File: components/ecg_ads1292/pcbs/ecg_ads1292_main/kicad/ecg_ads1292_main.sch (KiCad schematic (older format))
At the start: 13 parts, among them J1 Conn_02x04_Odd_Even, P1 Conn_02x20_Odd_Even

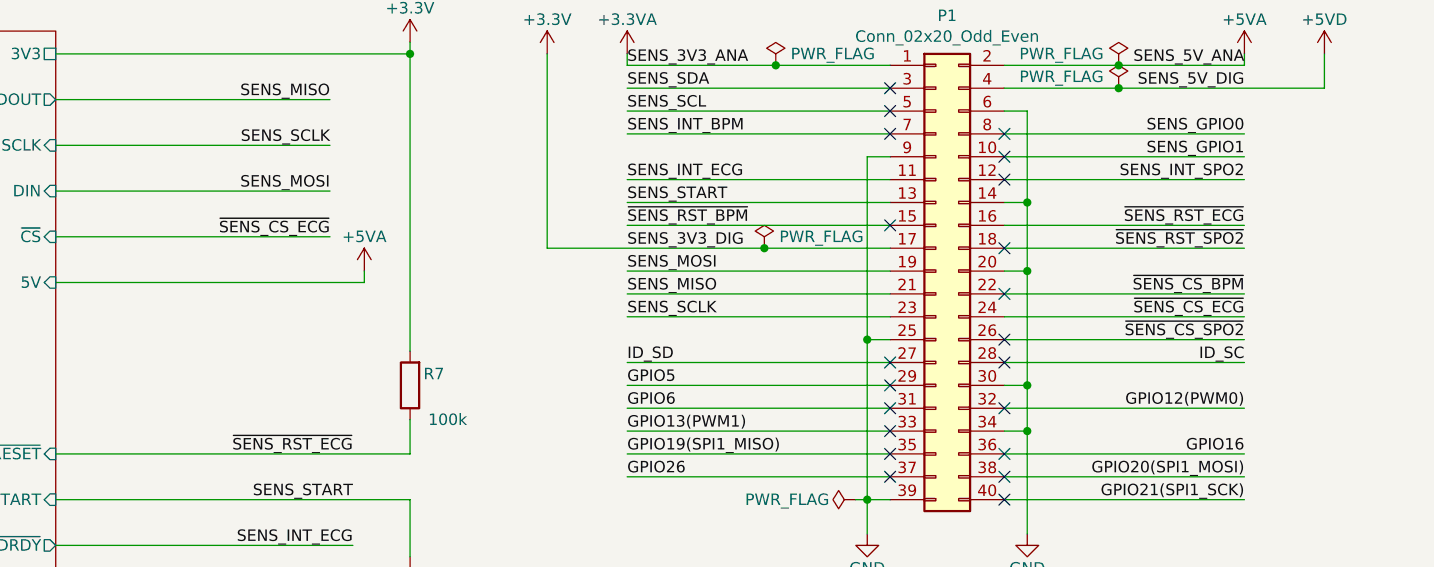
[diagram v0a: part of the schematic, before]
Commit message: add chip select mux in ads1292_main schematics
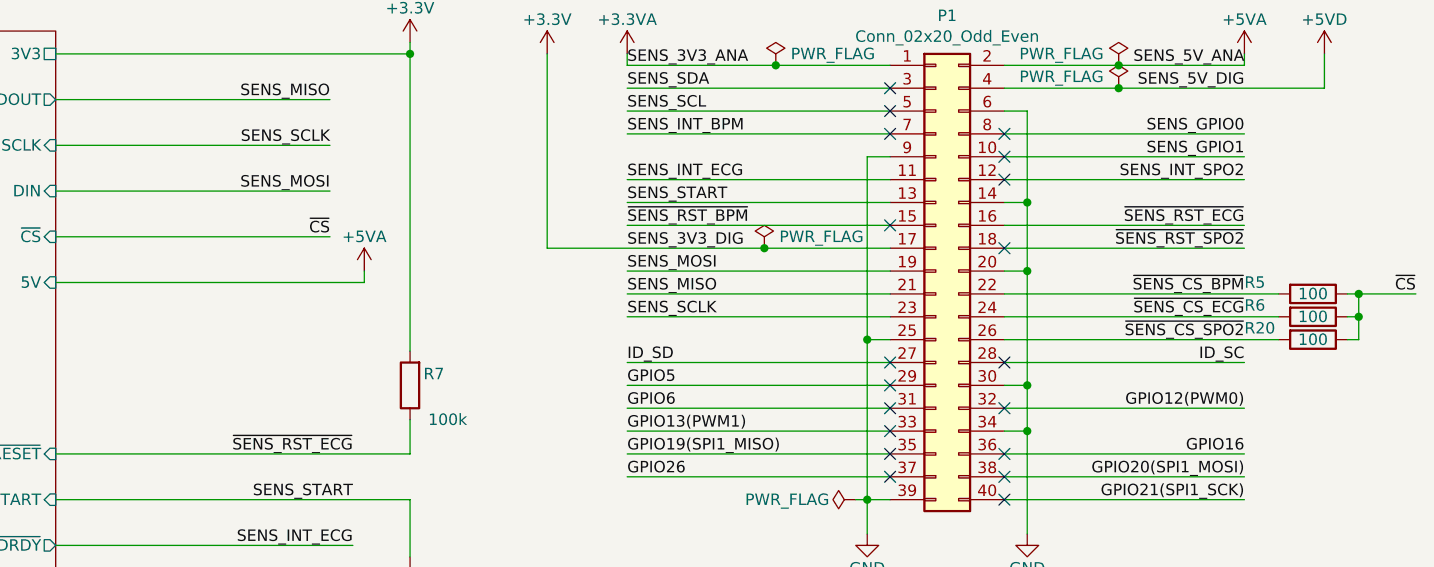
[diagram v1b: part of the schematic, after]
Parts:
- added R20, R5, R6: 100, Resistor_SMD:R_0603_1608Metric_Pad1.05x0.95mm_HandSolder, symbol component:R
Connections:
- net ~SENS_CS_BPM: now also R5.2
- net ~SENS_CS_ECG: now also R6.2
- net ~SENS_CS_SPO2: now also R20.2
- new net ~CS: R20.1, R5.1, R6.1
- no-connect marks 21 -> 19
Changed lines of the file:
@@
 Sheet 1 2
 Title "lifesensor ecg ads1292 main"
-Date "2020-04-27"
+Date "2020-04-28"
 Rev "1"
 Comp "Cadus e.V."
@@
 	14150 4250 15200 4250
 Wire Wire Line
-	14150 3650 15200 3650
-Wire Wire Line
 	14150 3750 15200 3750
-Wire Wire Line
-	14150 3450 15200 3450
-Wire Wire Line
-	14150 3550 15200 3550
 Wire Wire Line
 	14150 3150 15200 3150
@@
 Text Notes 13400 5800 0    50   ~ 0
 Mounting Holes
-$Comp
-L Connector_Generic:Conn_02x20_Odd_Even P1
-U 1 1 59AD464A
-P 13850 3350
-F 0 "P1" H 13900 4467 50  0000 C CNN
-F 1 "Conn_02x20_Odd_Even" H 13900 4376 50  0000 C CNN
-F 2 "Connector_PinSocket_2.54mm:PinSocket_2x20_P2.54mm_Vertical" H 9000 2400 50  0001 C CNN
-F 3 "" H 9000 2400 50  0001 C CNN
-	1    13850 3350
-	1    0    0    -1
-$EndComp
 Wire Wire Line
 	14150 4350 15200 4350
@@
 	11350 3350 11350 3400
 Text Label 11200 3200 2    50   ~ 0
-~SENS_CS_ECG
+~CS
 Text Label 7600 3000 2    50   ~ 0
 LA
@@
 NoConn ~ 13650 3150
 NoConn ~ 14150 3250
-NoConn ~ 14150 3450
-NoConn ~ 14150 3650
 NoConn ~ 14150 3750
 NoConn ~ 13650 3750
@@
 Wire Wire Line
 	13500 4350 13550 4350
+$Comp
+L component:R R?
+U 1 1 5EA92C2C
+P 15500 3450
+AR Path="/5E8EE786/5EA92C2C" Ref="R?"  Part="1"
+AR Path="/5EA92C2C" Ref="R5"  Part="1"
+F 0 "R5" V 15450 3150 50  0000 L CNN
+F 1 "100" V 15500 3450 50  0000 C CNN
+F 2 "Resistor_SMD:R_0603_1608Metric_Pad1.05x0.95mm_HandSolder" V 15430 3450 50  0001 C CNN
+F 3 "" H 15500 3450 50  0001 C CNN
+F 4 "1739145" H 8050 450 50  0001 C CNN "Best.Nr."
+F 5 "Farnell" H 8050 450 50  0001 C CNN "Distributor"
+F 6 "1739145" H 8050 450 50  0001 C CNN "Farnell"
+	1    15500 3450
+	0    1    1    0
+$EndComp
+Wire Wire Line
+	14150 3450 15350 3450
+$Comp
+L component:R R?
+U 1 1 5EA9C980
+P 15500 3550
+AR Path="/5E8EE786/5EA9C980" Ref="R?"  Part="1"
+AR Path="/5EA9C980" Ref="R6"  Part="1"
+F 0 "R6" V 15450 3250 50  0000 L CNN
+F 1 "100" V 15500 3550 50  0000 C CNN
+F 2 "Resistor_SMD:R_0603_1608Metric_Pad1.05x0.95mm_HandSolder" V 15430 3550 50  0001 C CNN
+F 3 "" H 15500 3550 50  0001 C CNN
+F 4 "1739145" H 8050 550 50  0001 C CNN "Best.Nr."
+F 5 "Farnell" H 8050 550 50  0001 C CNN "Distributor"
+F 6 "1739145" H 8050 550 50  0001 C CNN "Farnell"
+	1    15500 3550
+	0    1    1    0
+$EndComp
+$Comp
+L component:R R?
+U 1 1 5EA9D0F1
+P 15500 3650
+AR Path="/5E8EE786/5EA9D0F1" Ref="R?"  Part="1"
+AR Path="/5EA9D0F1" Ref="R20"  Part="1"
+F 0 "R20" V 15450 3350 50  0000 L CNN
+F 1 "100" V 15500 3650 50  0000 C CNN
+F 2 "Resistor_SMD:R_0603_1608Metric_Pad1.05x0.95mm_HandSolder" V 15430 3650 50  0001 C CNN
+F 3 "" H 15500 3650 50  0001 C CNN
+F 4 "1739145" H 8050 650 50  0001 C CNN "Best.Nr."
+F 5 "Farnell" H 8050 650 50  0001 C CNN "Distributor"
+F 6 "1739145" H 8050 650 50  0001 C CNN "Farnell"
+	1    15500 3650
+	0    1    1    0
+$EndComp
+Wire Wire Line
+	14150 3550 15350 3550
+Wire Wire Line
+	14150 3650 15350 3650
+Wire Wire Line
+	15650 3650 15700 3650
+Wire Wire Line
+	15700 3650 15700 3550
+Wire Wire Line
+	15700 3450 15950 3450
+Wire Wire Line
+	15700 3450 15650 3450
+Connection ~ 15700 3450
+Wire Wire Line
+	15650 3550 15700 3550
+Connection ~ 15700 3550
+Wire Wire Line
+	15700 3550 15700 3450
+Text Label 15950 3450 2    50   ~ 0
+~CS
+$Comp
+L Connector_Generic:Conn_02x20_Odd_Even P1
+U 1 1 59AD464A
+P 13850 3350
+F 0 "P1" H 13900 4467 50  0000 C CNN
+F 1 "Conn_02x20_Odd_Even" H 13900 4376 50  0000 C CNN
+F 2 "Connector_PinSocket_2.54mm:PinSocket_2x20_P2.54mm_Vertical" H 9000 2400 50  0001 C CNN
+F 3 "" H 9000 2400 50  0001 C CNN
+	1    13850 3350
+	1    0    0    -1
+$EndComp
 $EndSCHEMATC

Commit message: ecg_ads1292: fix symbol library paths
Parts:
- R1, R2, R20, R3, R5, R6, R7, R8: symbol component:R -> ecg_ads1292_main:R
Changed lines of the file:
@@
 	11550 4150 11550 4000
 $Comp
-L component:R R?
+L ecg_ads1292_main:R R?
 U 1 1 5EAAA6B2
 P 11550 4750
@@
 	11550 4350 11550 4600
 $Comp
-L component:R R?
+L ecg_ads1292_main:R R?
 U 1 1 5EAA9ADF
 P 11550 3850
@@
 $EndComp
 $Comp
-L component:GND #PWR?
+L ecg_ads1292_main:GND #PWR?
 U 1 1 5EB1856C
 P 10600 4950
@@
 RLD
 $Comp
-L component:GND #PWR?
+L ecg_ads1292_main:GND #PWR?
 U 1 1 5EC2A850
 P 11550 4950
@@
 $EndComp
 $Comp
-L component:GND #PWR?
+L ecg_ads1292_main:GND #PWR?
 U 1 1 5EB18F02
 P 7650 4500
@@
 	6800 4050 6800 4450
 $Comp
-L component:R R2
+L ecg_ads1292_main:R R2
 U 1 1 5E89C150
 P 7000 4050
@@
 	7150 4050 7200 4050
 $Comp
-L component:R R1
+L ecg_ads1292_main:R R1
 U 1 1 5E9D9425
 P 7000 3650
@@
 Connection ~ 7200 4050
 $Comp
-L component:R R3
+L ecg_ads1292_main:R R3
 U 1 1 5E89BC88
 P 7000 4450
@@
 Connection ~ 6800 4450
 $Comp
-L component:GND #PWR02
+L ecg_ads1292_main:GND #PWR02
 U 1 1 5E899B61
 P 7200 4550
@@
 	13500 4350 13550 4350
 $Comp
-L component:R R?
+L ecg_ads1292_main:R R?
 U 1 1 5EA92C2C
 P 15500 3450
@@
 	14150 3450 15350 3450
 $Comp
-L component:R R?
+L ecg_ads1292_main:R R?
 U 1 1 5EA9C980
 P 15500 3550
@@
 $EndComp
 $Comp
-L component:R R?
+L ecg_ads1292_main:R R?
 U 1 1 5EA9D0F1
 P 15500 3650

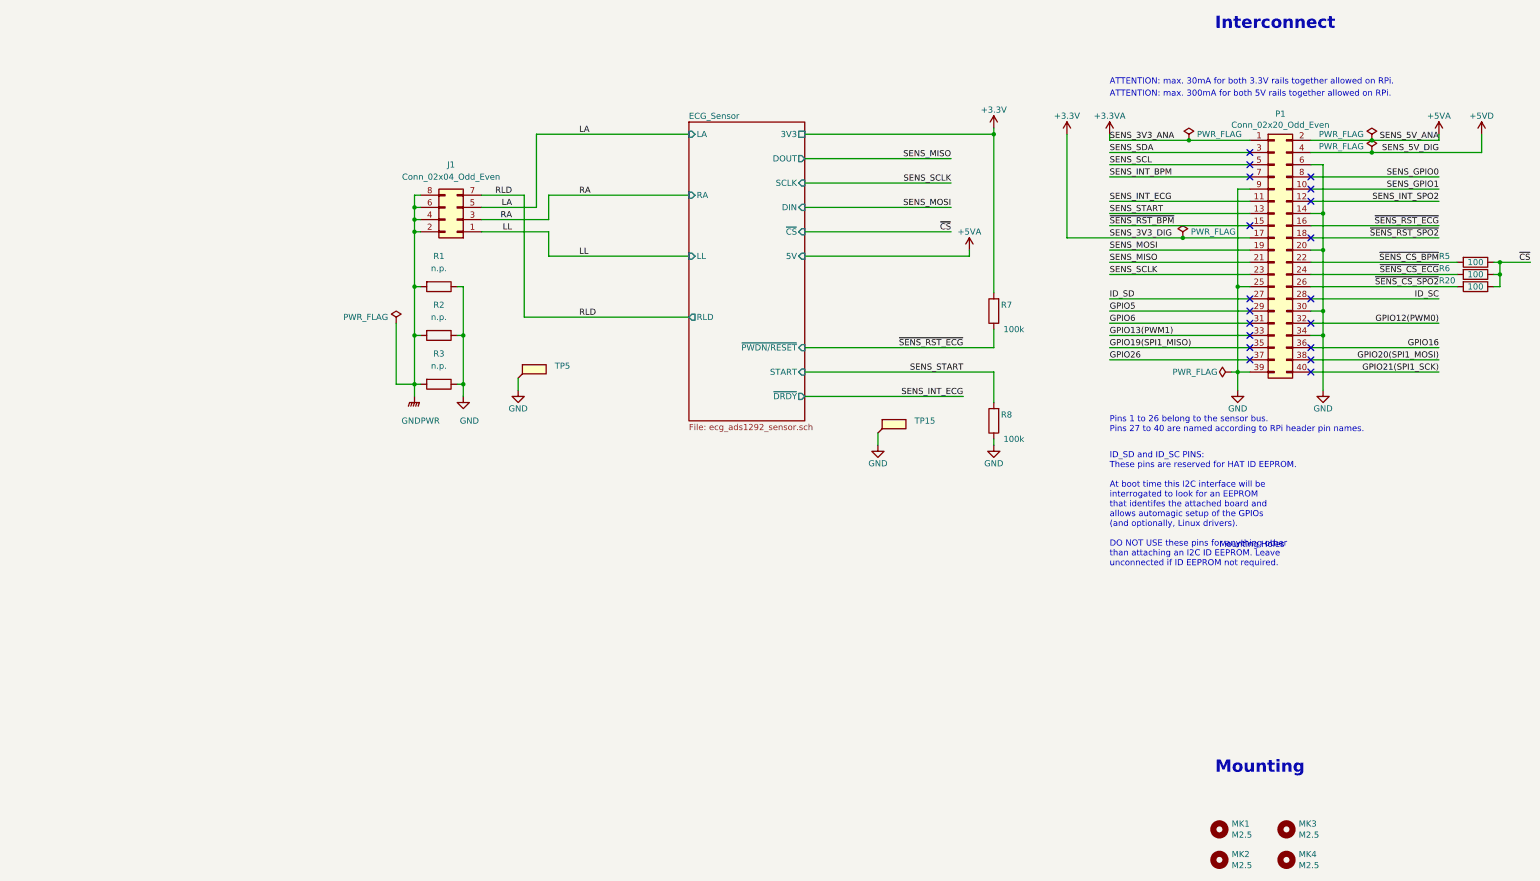
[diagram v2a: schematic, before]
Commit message: ecg_ads1292: update part fields
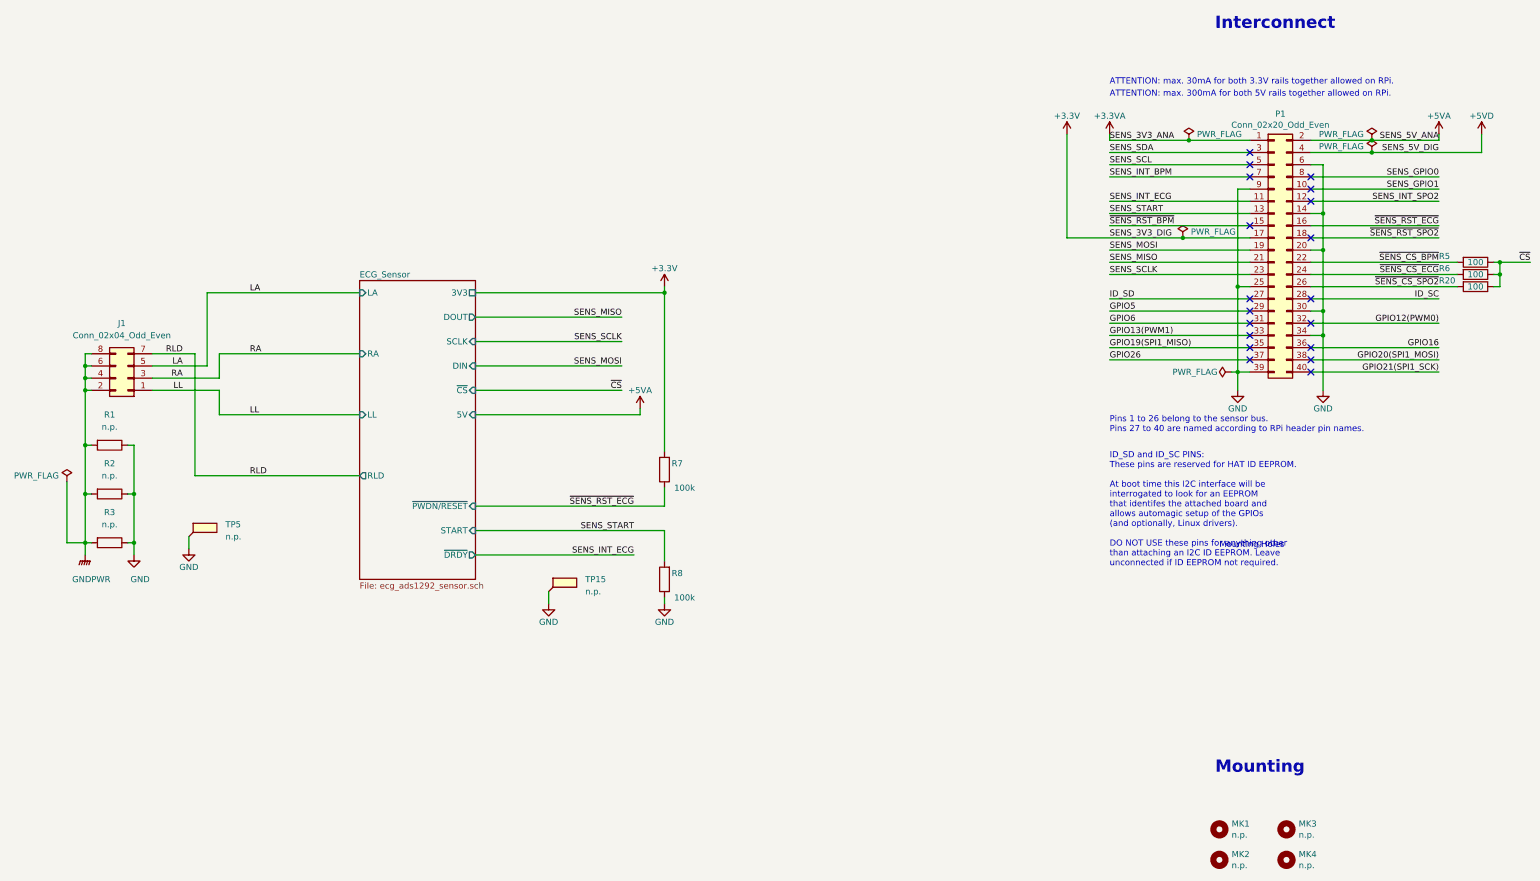
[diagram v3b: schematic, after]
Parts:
- J1: PN Farnell (none) -> 2856699
- MK1, MK2, MK3, MK4: value M2.5 -> n.p.
- R20, R5, R6: Best.Nr. 1739145 -> (none); Distributor Farnell -> (none); Farnell 1739145 -> (none); PN Farnell (none) -> 1739145
- R7, R8: Best.Nr. 1738916 -> (none); Distributor Farnell -> (none); Farnell 1738916 -> (none); PN Farnell (none) -> 1738916
- TP15, TP5: value (none) -> n.p.
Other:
- moved on the sheet: J1, R1, R2, R3, R7, R8, TP15, TP5
